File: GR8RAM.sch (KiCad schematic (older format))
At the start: 36 parts, among them J1 AppleIIBus, J2 JTAG, U1 EPM7128SL84, U5 39F040

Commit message: Release candidate PCB
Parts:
- removed C15: 100n, stdpads:C_0805, symbol Device:C_Small
- removed C18: 33u, stdpads:CP_EIA-3528, symbol Device:CP_Small
- removed FD1, FD2, FD3, FD4, FD5: Fiducial, stdpads:Fiducial, symbol Mechanical:MountingHole
- added C13, C18, C21, C22: 100n, stdpads:C_0805, symbol Device:C_Small
- added C15, C16: 33u, stdpads:CP_EIA-3528, symbol Device:CP_Small
- added FID1, FID2, FID3, FID4, FID5: Fiducial, stdpads:Fiducial, symbol Mechanical:Fiducial
- added JP1: Mode, Connector_PinHeader_2.54mm:PinHeader_1x02_P2.54mm_Vertical_SMD_Pin1Left, symbol Device:Jumper_NO_Small
- added R1, R2, R3, R4: 100, stdpads:R_0805, symbol Device:R_Small
- added R5: 820, stdpads:R_0805, symbol Device:R_Small
- J2: footprint Connector_IDC:IDC-Header_2x05_P2.54mm_Vertical -> stdpads:IDC_SMD_2x05_P2.54mm_Vertical
- U1: footprint stdpads:PLCC-84 -> stdpads:PLCC-84_SMDSocket
- U2: renamed from U5; footprint stdpads:PLCC-32 -> stdpads:PLCC-32_SMDSocket
- U3, U4, U5, U6: renamed from U?; footprint Package_SO:TSOP-II-44_10.16x18.41mm_P0.8mm -> stdpads:SOP-24-26-300mil
- renumbered C16 to C14
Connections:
- net labels added: 7Mr, PHI0r, PHI1r, Q3r, R~CS~, R~OE~, ~CAS~0, ~CAS~1, ~MODE~
- net labels removed: RAMROM~CS~gb, ROM~OE~, ROM~WE~, ~CAS~
- wire segments 113 -> 162
- no-connect marks 5 -> 6
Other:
- note added: "CSEN = S1 | S2 | S3 @ ~C7M~\nR~WE~ovrd = S4 | S5 | S6 @ C7M\n\nRD[7:0] = ~R~W ? D[7:0] : 8’bZ\nD[7:0] = (~CSEN~ | ~DEVSEL~ | ~R~W) ? 8’bZ :\n ADDRHI ? {1’b1, AR[22:16]} : \n ADDRMED ? AR[15:8] : \n ADDRLO ? AR[7:0] : \n RD[7:0]\n\nRA[10:8] = S1 ? AR[10:8] : AR[21:19] @ C7M\nRA[7:0] = RAMREG ? (S1 ? AR[7:0] : AR[18:11]) : \n IOSEL ? 8’b00 : Bank[7:0] @ C7M\n\nROMCS = IOSEL | (IOSTRB & ROMEN)\nR~WE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"
- note added: "R~WE~ovrd"
- note added: "S[2:0] = (S == 0) ? 0 : (~Q3~ & PHI1) ? 1 : S+1 @ C7M\n\nBANKREG = (A==C0XF) & DEVSEL & REGEN @ C7M in S7\nRAMREG = (A==C0X3) & DEVSEL & REGEN @ C7M in S7\nADDRHI = (A==C0X2) & DEVSEL & REGEN @ C7M in S7\nADDRMD = (A==C0X1) & DEVSEL & REGEN @ C7M in S7\nADDRLO = (A==C0X0) & DEVSEL & REGEN @ C7M in S7\n\nREGEN = IOSEL ? 1 : REGEN @ C7M in S7\nROMEN = (A==CFFF) ? 0 :\n (A==CX00 & IOSEL) ? 1 :\n IOR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"
- note added: "~CAS~"
- note added: "~RAS~"
- note removed: "CSEN = S1 | S2 | S3 @ C7M\n\nD[7:0] = (~CSEN~ | ~DEVSEL~ | ~R~W) ? 8’bZ :\n BANKREG ? Bank[5:0]\n ADDRHI ? {4’hF, AR[19:16]} : \n ADDRMED ? AR[15:8] : \n ADDRLO ? AR[7:0]\n\nRA[19] = AR[19]\nRA[18:12] = RAMREG ? AR[18:12] : { SyncCnt[2:0]!=0, Bank[5:0] }\nRA[11:0] = AR[11:0]\n\nRAMROM~CS~ = ~IOSEL or IOSTRB~\nRAMCS = CSEN & RAMREG\nROM~OE~ = CSEN & (IOSEL | (IOSTRB & IOROMEN)) & R~W~\nROM~WE~ = C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"
- note removed: "S[2:0] = (S == 0) ? 0 : (~Q3~ & PHI1) ? 1 : S+1 @ C7M\n\nSyncCnt[1:0] = SYNC ? 2’b11 : \n SyncCnt==0 ? 0 :\n SyncCnt-1 @ C7M in S7\n\nBANKREG = (A==C0XF) & DEVSEL @ C7M in S7\nRAMREG = (A==C0X3) & DEVSEL @ C7M in S7\nADDRHI = (A==C0X2) & DEVSEL @ C7M in S7\nADDRMD = (A==C0X1) & DEVSEL @ C7M in S7\nADDRLO = (A==C0X0) & DEVSEL @ C7M in S7\n\nIOROMEN = (A==CFFF) ? 0 :\n (A==CX00 & IOSEL) ? 1 :\n IOR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"
- moved on the sheet: C1, C10, C11, C12, C14, C17, C19, C2, C20, C3, C4, C5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

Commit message: Submitted to JLCPCB
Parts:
- R5: value 820 -> 4k7
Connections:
- net labels added: VIDSYNC
- net labels removed: SYNC
- wire segments 162 -> 229
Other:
- note removed: "6502 CPU Access"
- note removed: "Allow CS, OE, WE"
- note removed: "C7M"
- note removed: "CSEN = S1 | S2 | S3 @ ~C7M~\nR~WE~ovrd = S4 | S5 | S6 @ C7M\n\nRD[7:0] = ~R~W ? D[7:0] : 8’bZ\nD[7:0] = (~CSEN~ | ~DEVSEL~ | ~R~W) ? 8’bZ :\n ADDRHI ? {1’b1, AR[22:16]} : \n ADDRMED ? AR[15:8] : \n ADDRLO ? AR[7:0] : \n RD[7:0]\n\nRA[10:8] = S1 ? AR[10:8] : AR[21:19] @ C7M\nRA[7:0] = RAMREG ? (S1 ? AR[7:0] : AR[18:11]) : \n IOSEL ? 8’b00 : Bank[7:0] @ C7M\n\nROMCS = IOSEL | (IOSTRB & ROMEN)\nR~WE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"
- note removed: "Disallow CS, OE, WE\nIncrement addr. if attr."
- note removed: "Latch WR data"
- note removed: "Latch addr. attr.\nSwitch ext. ROM"
- note removed: "PHI0"
- note removed: "PHI1"
- note removed: "Q3"
- note removed: "R~WE~ovrd"
- note removed: "S1"
- note removed: "S2"
- note removed: "S3"
- note removed: "S4"
- note removed: "S5"
- note removed: "S6"
- note removed: "S7"
- note removed: "S[2:0] = (S == 0) ? 0 : (~Q3~ & PHI1) ? 1 : S+1 @ C7M\n\nBANKREG = (A==C0XF) & DEVSEL & REGEN @ C7M in S7\nRAMREG = (A==C0X3) & DEVSEL & REGEN @ C7M in S7\nADDRHI = (A==C0X2) & DEVSEL & REGEN @ C7M in S7\nADDRMD = (A==C0X1) & DEVSEL & REGEN @ C7M in S7\nADDRLO = (A==C0X0) & DEVSEL & REGEN @ C7M in S7\n\nREGEN = IOSEL ? 1 : REGEN @ C7M in S7\nROMEN = (A==CFFF) ? 0 :\n (A==CX00 & IOSEL) ? 1 :\n IOR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"
- note removed: "Video Access"
- note removed: "~CAS~"
- note removed: "~RAS~"
- moved on the sheet: C1, C10, C11, C12, C13, C14, C15, C16, C17, C18, C19, C2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

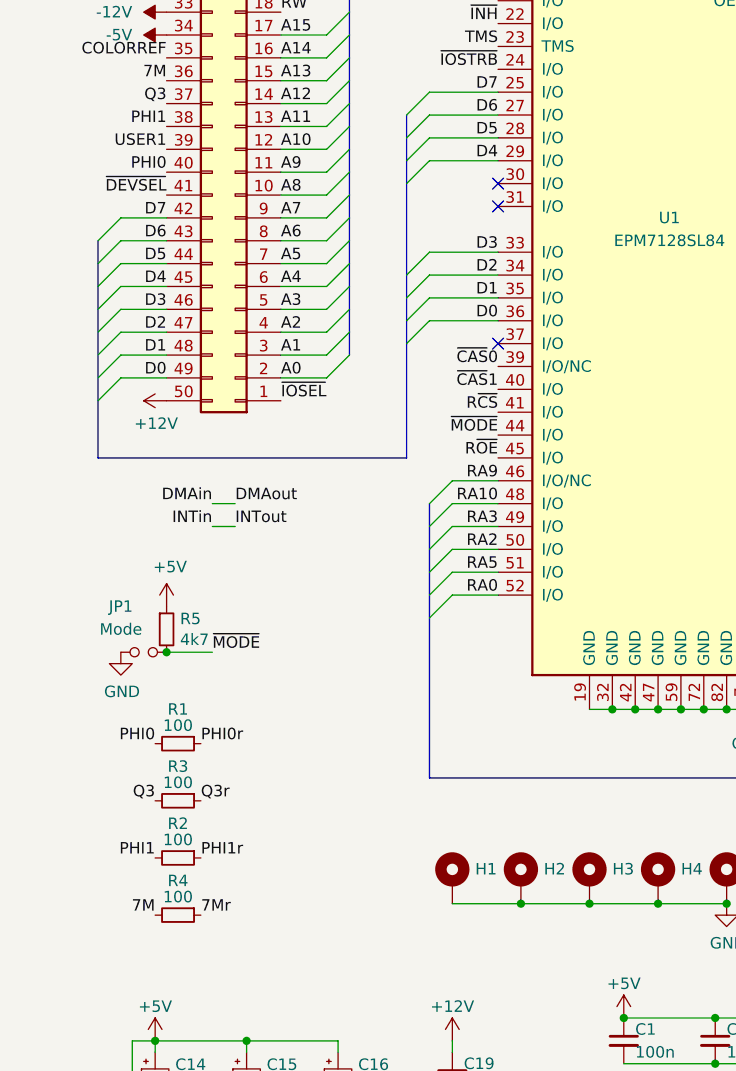
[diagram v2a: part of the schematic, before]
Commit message: CPLD firmware compiles
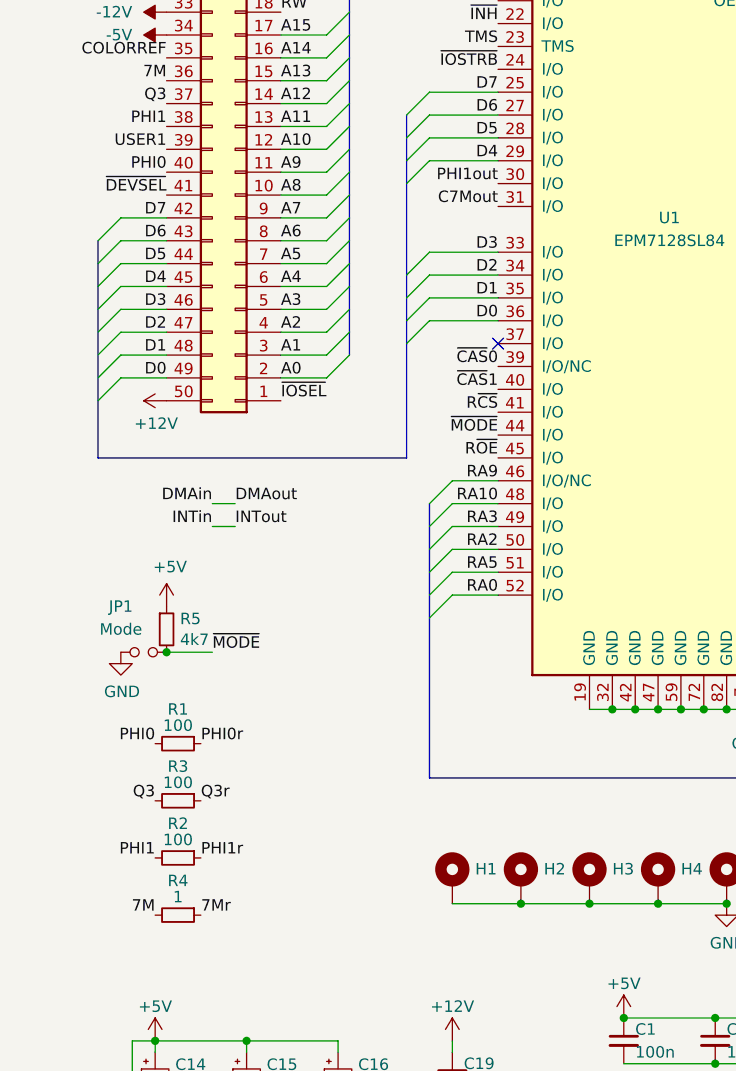
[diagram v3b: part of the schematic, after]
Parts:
- R4: value 100 -> 1
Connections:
- net PHI1out: now reaches U1.30 (I/O)
- net C7Mout: now reaches U1.31 (I/O)
- no-connect marks 6 -> 4
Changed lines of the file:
@@
 P 1300 6450
 F 0 "R4" V 1150 6450 50  0000 C CNN
-F 1 "100" V 1250 6450 50  0000 C BNN
+F 1 "1" V 1250 6450 50  0000 C BNN
 F 2 "stdpads:R_0805" H 1300 6450 50  0001 C CNN
 F 3 "~" H 1300 6450 50  0001 C CNN
@@
 	1    0    0    -1
 $EndComp
-NoConn ~ 2700 3250
-NoConn ~ 2700 3350
 NoConn ~ 2700 3950
 $Comp
@@
 Wire Bus Line
 	7300 1900 7300 5850
+Text Label 2700 3350 2    50   ~ 0
+C7Mout
+Text Label 2700 3250 2    50   ~ 0
+PHI1out
 $EndSCHEMATC
